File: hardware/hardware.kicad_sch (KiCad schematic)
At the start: 3 parts, among them J2 USB_C_Receptacle

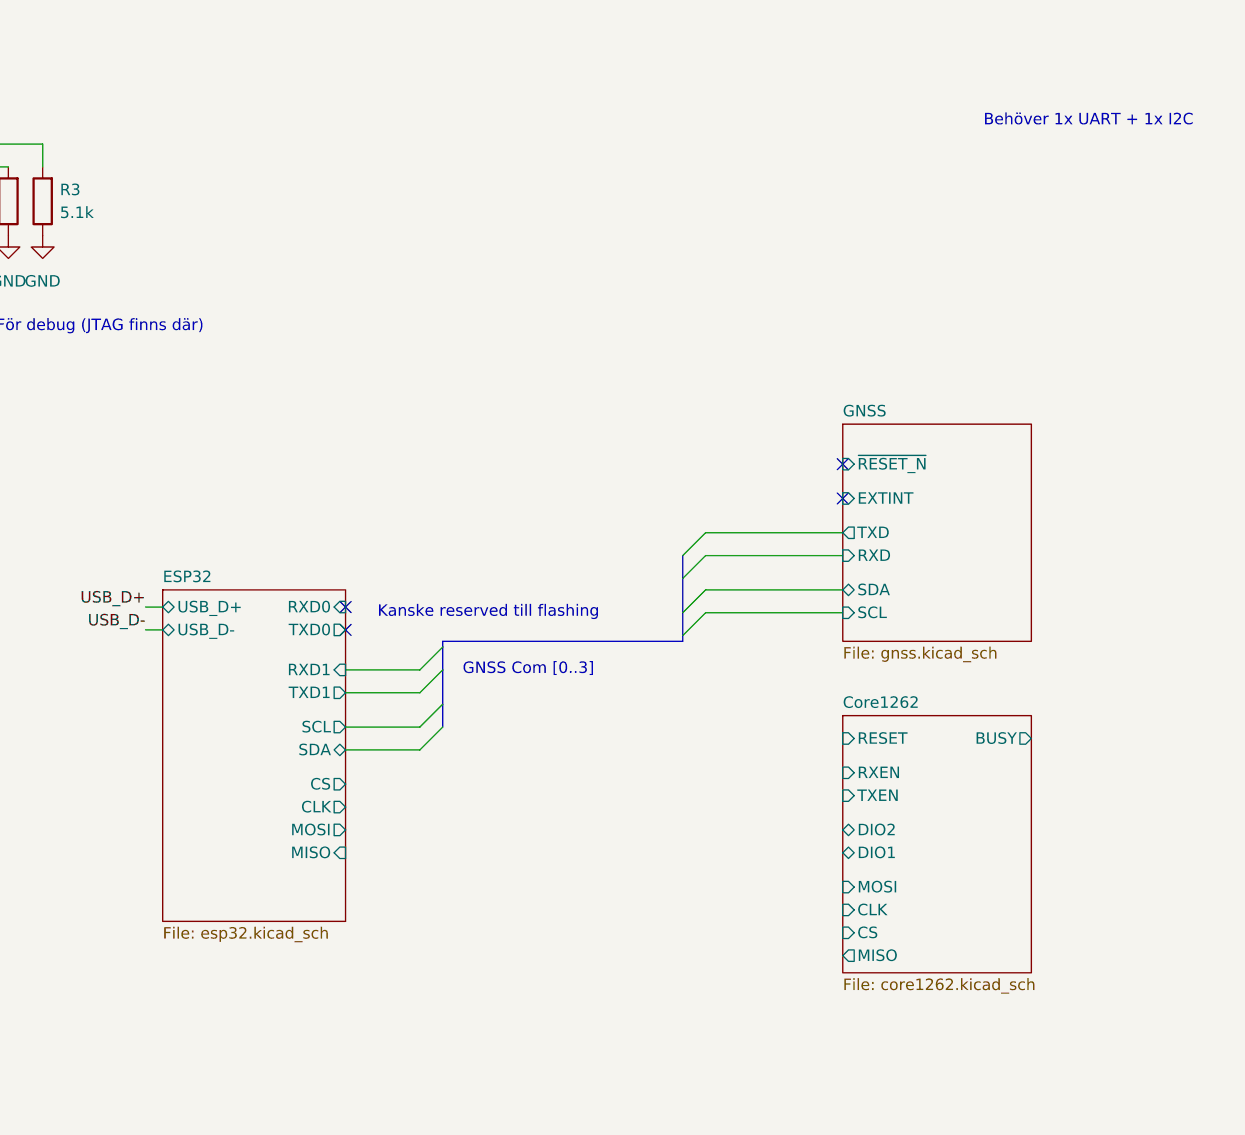
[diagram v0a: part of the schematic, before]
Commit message: drew more busses and connections
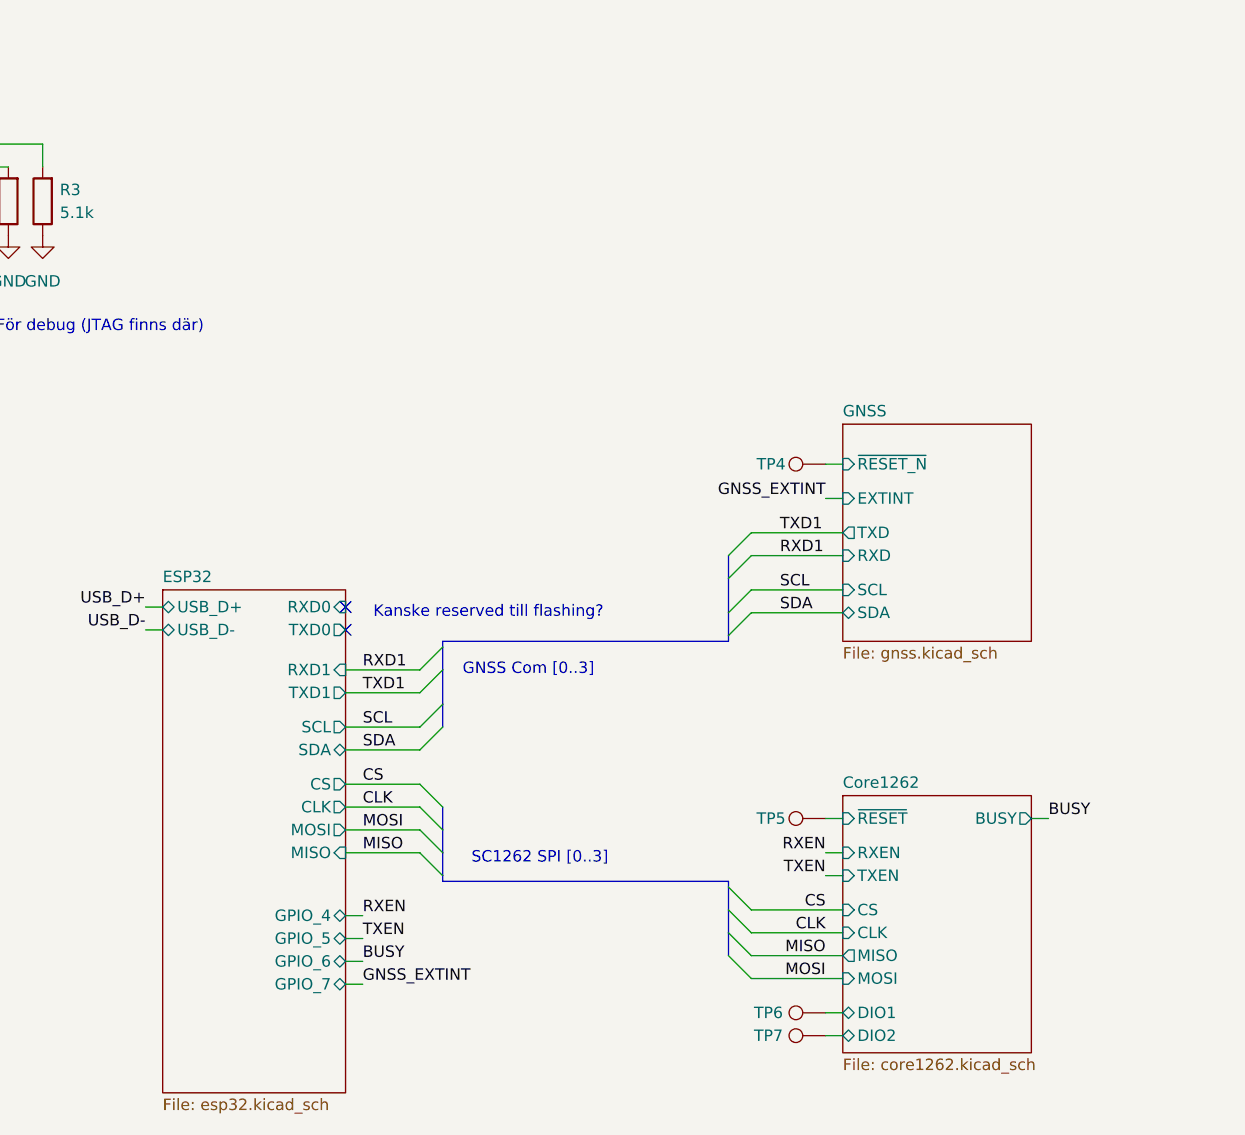
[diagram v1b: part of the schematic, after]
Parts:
- added TP4, TP5, TP6, TP7: TestPoint, symbol Connector:TestPoint
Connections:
- net Core1262/DIO1: now also TP6.1
- net Core1262/DIO2: now also TP7.1
- net GNSS/~{RESET_N}: now also TP4.1
- new net Core1262/~{RESET}: TP5.1
- no-connect marks 6 -> 4
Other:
- sheet Core1262 ports: added ~{RESET}; removed RESET
- sheet ESP32 ports: added GPIO_4, GPIO_5, GPIO_6, GPIO_7; removed none
- note added: "Kanske reserved till flashing?"
- note added: "SC1262 SPI [0..3]"
- note removed: "Behöver 1x UART + 1x I2C"
- note removed: "Kanske reserved till flashing"

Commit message: beginnings of power distribution maybe?
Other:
- moved on the sheet: TP4, TP5, TP6, TP7

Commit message: moved stuff around
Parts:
- added TP8, TP9: TestPoint, symbol Connector:TestPoint
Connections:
- net ESP32/RXD0: now also TP8.1
- net ESP32/TXD0: now also TP9.1
- no-connect marks 4 -> 2
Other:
- moved on the sheet: TP4, TP5, TP6, TP7
